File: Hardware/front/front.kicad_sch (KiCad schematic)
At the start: 53 parts, among them J101 Conn_02x10_Odd_Even, SW101 Alps EC11E, SW102 C&K-D6R-Illuminated, SW103 B3W-9002-Y1C, SW104 B3W-9002-Y1C, SW105 B3W-9002-Y1C, SW106 B3W-9002-Y1C, SW107 B3W-9000-RHG2C, U101 XRA1203, U102 AT24CS32-SSHM, U103 PCA9955B, U104 74LV14

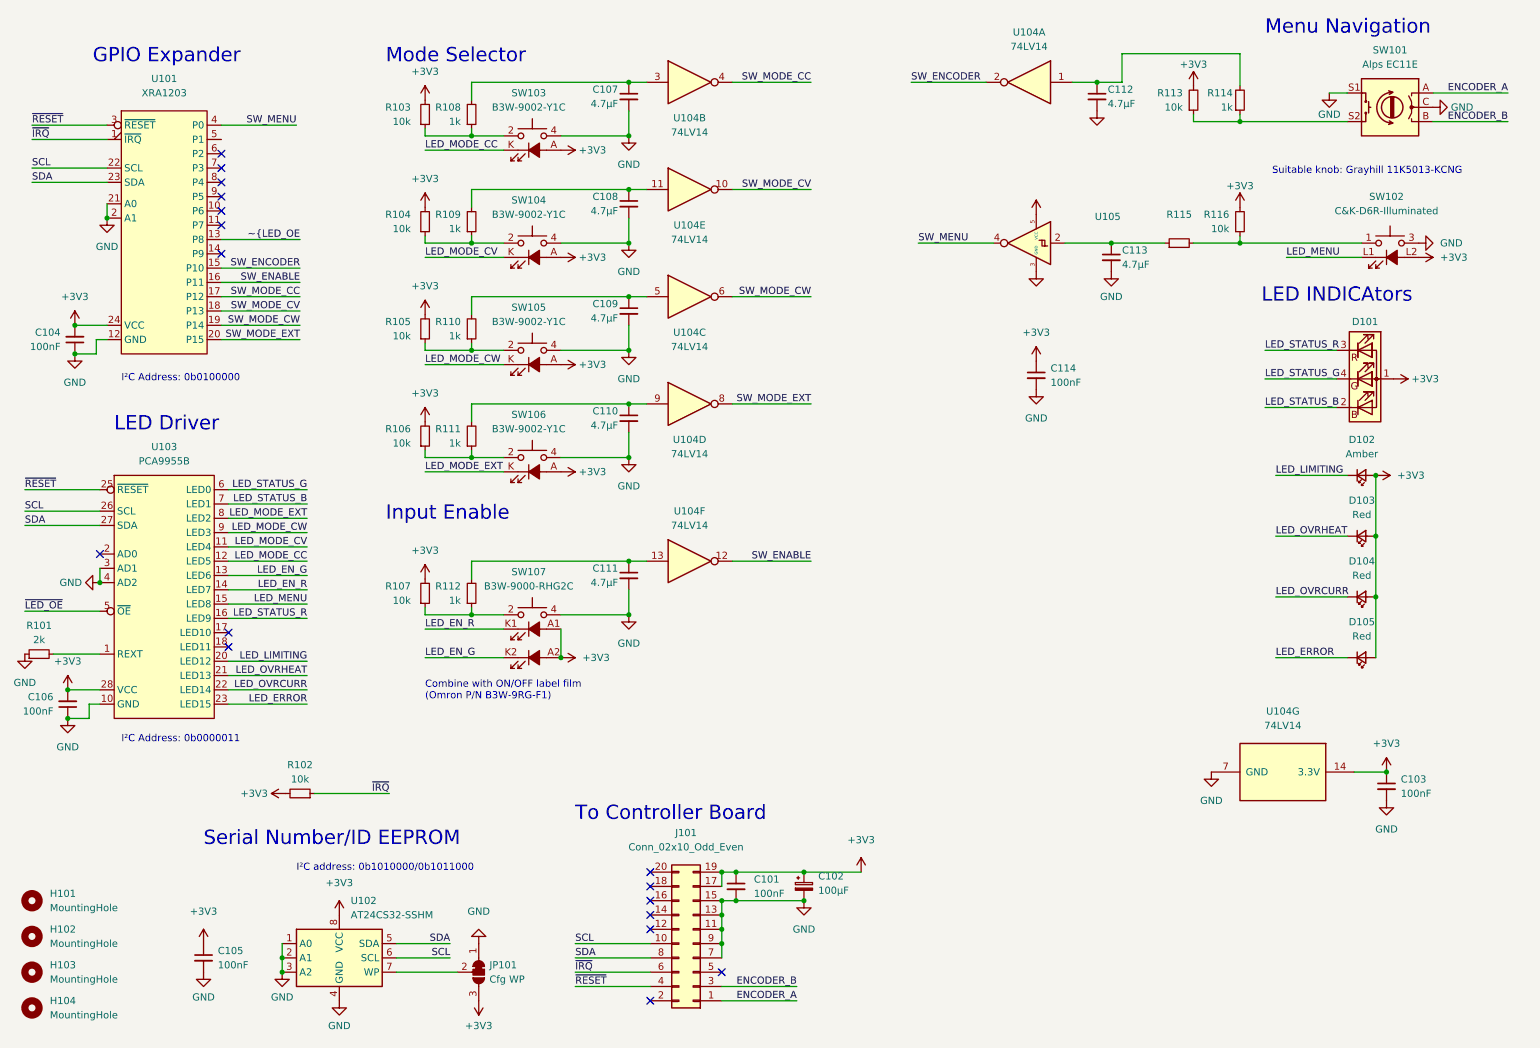
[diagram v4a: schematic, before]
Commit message: More tweaks to rev 2 front panel
- Added on-board pull ups for encoder lines, to reduce noise carried on
  the lines

- Cleaned up a few traces

- Actually fixed the footprint of the RGB LED so that not only does the
  common terminal match up, as do all three of the color terminals also
  :D
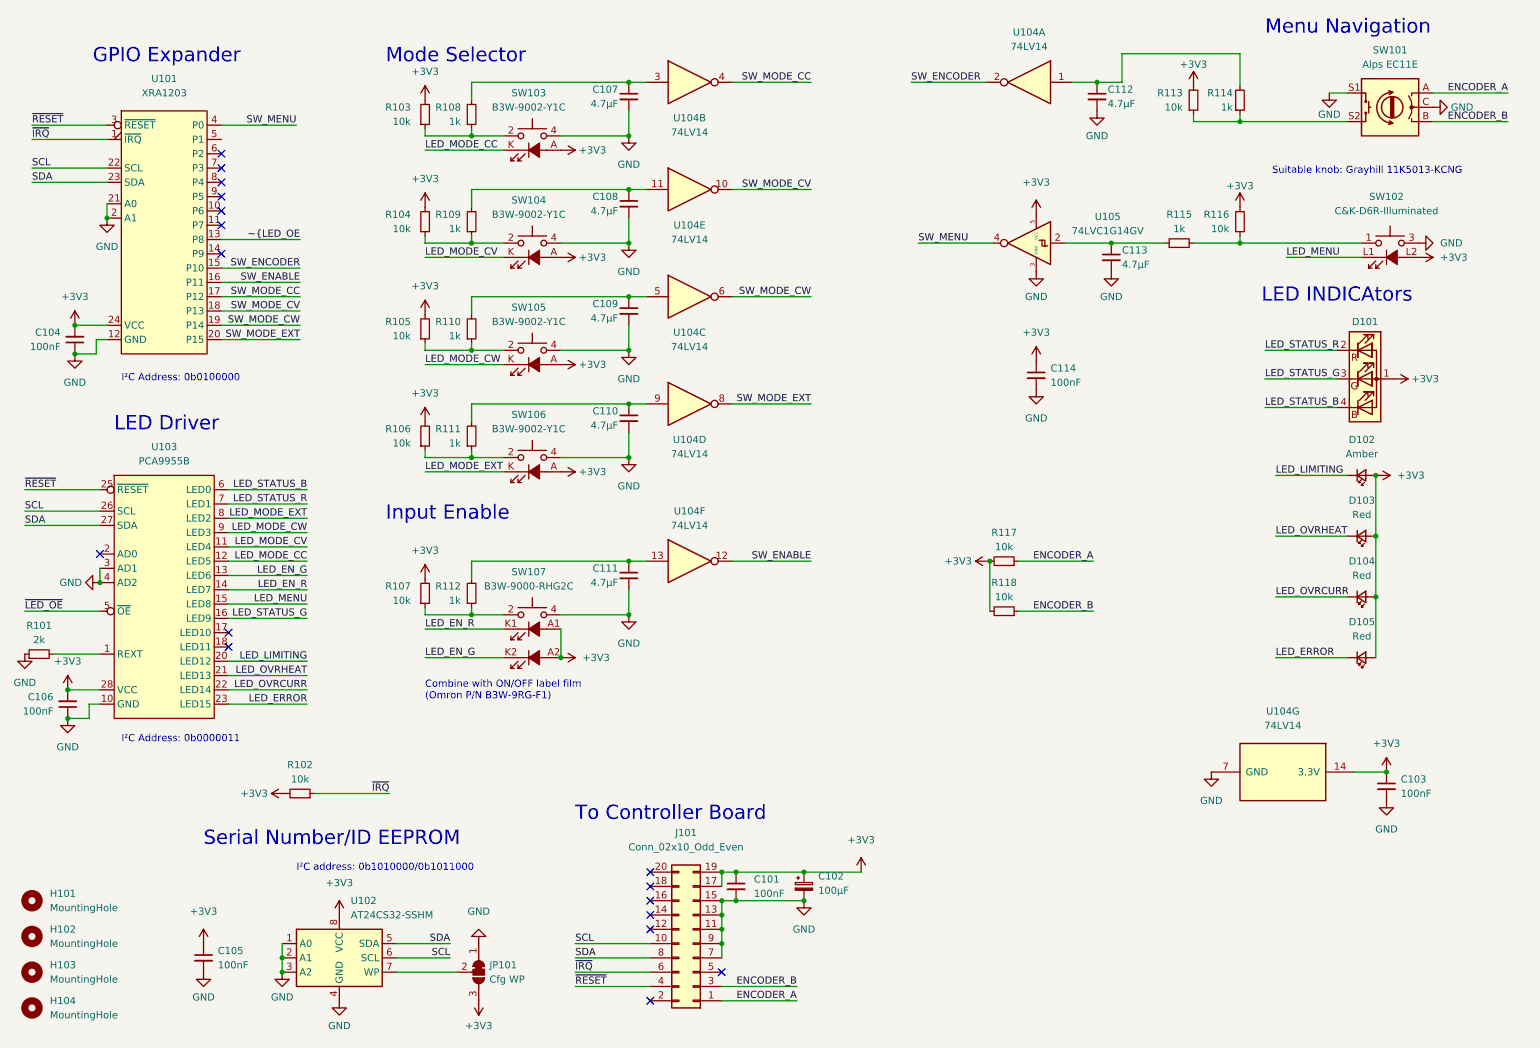
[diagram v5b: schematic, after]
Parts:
- added R117, R118: 10k, Resistor_SMD:R_0805_2012Metric_Pad1.20x1.40mm_HandSolder, symbol Device:R_Small
- D101: symbol Device:LED_ABRG -> Device:LED_ARGB
- R115: value (none) -> 1k; footprint (none) -> Resistor_SMD:R_0805_2012Metric_Pad1.20x1.40mm_HandSolder
- U105: value (none) -> 74LVC1G14GV; footprint (none) -> Package_TO_SOT_SMD:SOT-23-5
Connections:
- net +3V3: now also R117.2, R118.2
- net ENCODER_A: now also R117.1
- net ENCODER_B: now also R118.1
- net LED_STATUS_B: now also D101.4 (BK), U103.6 (LED0); no longer D101.2 (BK), U103.7 (LED1)
- net LED_STATUS_G: now also D101.3 (GK), U103.16 (LED9); no longer D101.4 (GK), U103.6 (LED0)
- net LED_STATUS_R: now also D101.2 (RK), U103.7 (LED1); no longer D101.3 (RK), U103.16 (LED9)
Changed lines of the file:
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@@
     (rev "1")
   )
+  (junction (at 189.23 111.125) (diameter 0) (color 0 0 0 0)
+  )
   (junction (at 97.155 35.56) (diameter 0) (color 0 0 0 0)
   )
@@
     (stroke (width 0) (type default) (color 0 0 0 0))
   )
+  (wire (pts (xy 207.645 111.125) (xy 194.31 111.125))
+    (stroke (width 0) (type default) (color 0 0 0 0))
+  )
   (wire (pts (xy 254 148.59) (xy 259.715 148.59))
     (stroke (width 0) (type default) (color 0 0 0 0))
@@
     (stroke (width 0) (type default) (color 0 0 0 0))
   )
+  (wire (pts (xy 189.23 111.125) (xy 189.23 120.015))
+    (stroke (width 0) (type default) (color 0 0 0 0))
+  )
   (wire (pts (xy 67.945 103.505) (xy 53.975 103.505))
     (stroke (width 0) (type default) (color 0 0 0 0))
@@
     (stroke (width 0) (type default) (color 0 0 0 0))
   )
+  (wire (pts (xy 207.645 120.015) (xy 194.31 120.015))
+    (stroke (width 0) (type default) (color 0 0 0 0))
+  )
   (wire (pts (xy 53.975 100.965) (xy 67.945 100.965))
     (stroke (width 0) (type default) (color 0 0 0 0))
@@
     (effects (font (size 1.27 1.27)) (justify left bottom))
   )
-  (label "LED_STATUS_B" (at 67.945 100.965 180)
+  (label "LED_STATUS_R" (at 67.945 100.965 180)
     (effects (font (size 1.27 1.27)) (justify right bottom))
   )
@@
     (effects (font (size 1.27 1.27)) (justify right bottom))
   )
+  (label "ENCODER_A" (at 207.645 111.125 180)
+    (effects (font (size 1.27 1.27)) (justify right bottom))
+  )
   (label "LED_LIMITING" (at 67.945 128.905 180)
     (effects (font (size 1.27 1.27)) (justify right bottom))
@@
     (effects (font (size 1.27 1.27)) (justify right bottom))
   )
-  (label "LED_STATUS_R" (at 67.945 121.285 180)
+  (label "LED_STATUS_G" (at 67.945 121.285 180)
     (effects (font (size 1.27 1.27)) (justify right bottom))
   )
@@
     (effects (font (size 1.27 1.27)) (justify left bottom))
   )
+  (label "ENCODER_B" (at 207.645 120.015 180)
+    (effects (font (size 1.27 1.27)) (justify right bottom))
+  )
   (label "SW_MODE_CW" (at 66.675 69.215 180)
     (effects (font (size 1.27 1.27)) (justify right bottom))
@@
     (effects (font (size 1.27 1.27)) (justify left bottom))
   )
-  (label "LED_STATUS_G" (at 67.945 98.425 180)
+  (label "LED_STATUS_B" (at 67.945 98.425 180)
     (effects (font (size 1.27 1.27)) (justify right bottom))
   )
@@
       (effects (font (size 1.27 1.27)) hide)
     )
-    (property "Value" "" (id 1) (at 197.485 43.815 0))
+    (property "Value" "+3V3" (id 1) (at 197.485 43.815 0))
     (property "Footprint" "" (id 2) (at 197.485 49.53 0)
       (effects (font (size 1.27 1.27)) hide)
@@
     (pin "2")
   )
-  (symbol (lib_id "Device:LED_ABRG") (at 255.905 78.74 0) (unit 1)
+  (symbol (lib_id "Device:LED_ARGB") (at 255.905 78.74 0) (unit 1)
     (in_bom yes) (on_board yes)
     (property "Reference" "D101" (id 0) (at 255.905 68.58 0))
@@
     (in_bom yes) (on_board yes) (fields_autoplaced)
     (property "Reference" "U105" (id 0) (at 210.185 49.911 0))
-    (property "Value" "" (id 1) (at 210.185 52.451 0))
-    (property "Footprint" "" (id 2) (at 197.485 60.96 0)
+    (property "Value" "74LVC1G14GV" (id 1) (at 210.185 52.451 0))
+    (property "Footprint" "Package_TO_SOT_SMD:SOT-23-5" (id 2) (at 197.485 60.96 0)
       (effects (font (size 1.27 1.27)) hide)
     )
@@
     (pin "1")
   )
+  (symbol (lib_id "power:+3V3") (at 189.23 111.125 90) (unit 1)
+    (in_bom yes) (on_board yes) (fields_autoplaced)
+    (property "Reference" "#PWR0150" (id 0) (at 193.04 111.125 0)
+      (effects (font (size 1.27 1.27)) hide)
+    )
+    (property "Value" "+3V3" (id 1) (at 186.055 111.1249 90)
+      (effects (font (size 1.27 1.27)) (justify left))
+    )
+    (property "Footprint" "" (id 2) (at 189.23 111.125 0)
+      (effects (font (size 1.27 1.27)) hide)
+    )
+    (property "Datasheet" "" (id 3) (at 189.23 111.125 0)
+      (effects (font (size 1.27 1.27)) hide)
+    )
+    (pin "1")
+  )
   (symbol (lib_id "programmable-load:XRA1203") (at 42.545 31.115 0) (unit 1)
     (in_bom yes) (on_board yes) (fields_autoplaced)
@@
     (in_bom yes) (on_board yes)
     (property "Reference" "R115" (id 0) (at 222.885 49.53 90))
-    (property "Value" "" (id 1) (at 222.885 52.07 90))
-    (property "Footprint" "" (id 2) (at 222.885 54.61 0)
+    (property "Value" "1k" (id 1) (at 222.885 52.07 90))
+    (property "Footprint" "Resistor_SMD:R_0805_2012Metric_Pad1.20x1.40mm_HandSolder" (id 2) (at 222.885 54.61 0)
       (effects (font (size 1.27 1.27)) hide)
     )
@@
     (pin "2")
   )
+  (symbol (lib_id "Device:R_Small") (at 191.77 120.015 270) (mirror x) (unit 1)
+    (in_bom yes) (on_board yes)
+    (property "Reference" "R118" (id 0) (at 191.77 114.935 90))
+    (property "Value" "10k" (id 1) (at 191.77 117.475 90))
+    (property "Footprint" "Resistor_SMD:R_0805_2012Metric_Pad1.20x1.40mm_HandSolder" (id 2) (at 191.77 120.015 0)
+      (effects (font (size 1.27 1.27)) hide)
+    )
+    (property "Datasheet" "~" (id 3) (at 191.77 120.015 0)
+      (effects (font (size 1.27 1.27)) hide)
+    )
+    (property "MPN" "RMC1/10-103JTP" (id 4) (at 191.77 120.015 90)
+      (effects (font (size 1.27 1.27)) hide)
+    )
+    (pin "1")
+    (pin "2")
+  )
   (symbol (lib_id "Device:C_Small") (at 210.82 57.15 0) (unit 1)
     (in_bom yes) (on_board yes)
@@
       (effects (font (size 1.27 1.27)) hide)
     )
-    (property "Value" "" (id 1) (at 197.485 64.135 0))
+    (property "Value" "GND" (id 1) (at 197.485 64.135 0))
     (property "Footprint" "" (id 2) (at 197.485 59.69 0)
       (effects (font (size 1.27 1.27)) hide)
@@
       (effects (font (size 1.27 1.27)) hide)
     )
-    (property "Value" "" (id 1) (at 208.28 35.56 0))
+    (property "Value" "GND" (id 1) (at 208.28 35.56 0))
     (property "Footprint" "" (id 2) (at 208.28 31.115 0)
       (effects (font (size 1.27 1.27)) hide)
@@
     (pin "2")
   )
+  (symbol (lib_id "Device:R_Small") (at 191.77 111.125 270) (mirror x) (unit 1)
+    (in_bom yes) (on_board yes)
+    (property "Reference" "R117" (id 0) (at 191.77 106.045 90))
+    (property "Value" "10k" (id 1) (at 191.77 108.585 90))
+    (property "Footprint" "Resistor_SMD:R_0805_2012Metric_Pad1.20x1.40mm_HandSolder" (id 2) (at 191.77 111.125 0)
+      (effects (font (size 1.27 1.27)) hide)
+    )
+    (property "Datasheet" "~" (id 3) (at 191.77 111.125 0)
+      (effects (font (size 1.27 1.27)) hide)
+    )
+    (property "MPN" "RMC1/10-103JTP" (id 4) (at 191.77 111.125 90)
+      (effects (font (size 1.27 1.27)) hide)
+    )
+    (pin "1")
+    (pin "2")
+  )
   (symbol (lib_id "power:GND") (at 31.115 114.935 270) (unit 1)
     (in_bom yes) (on_board yes) (fields_autoplaced)
@@
       (reference "#PWR0149") (unit 1) (value "GND") (footprint "")
     )
+    (path "/68dadee9-22bb-4cbe-aa25-79886e75d180"
+      (reference "#PWR0150") (unit 1) (value "+3V3") (footprint "")
+    )
     (path "/41415bac-1126-4467-b765-03fce423d075"
       (reference "C101") (unit 1) (value "100nF") (footprint "Capacitor_SMD:C_0805_2012Metric_Pad1.18x1.45mm_HandSolder")
@@
       (reference "R116") (unit 1) (value "10k") (footprint "Resistor_SMD:R_0805_2012Metric_Pad1.20x1.40mm_HandSolder")
     )
+    (path "/d7068e86-6312-4342-aa63-c1b7ad68015f"
+      (reference "R117") (unit 1) (value "10k") (footprint "Resistor_SMD:R_0805_2012Metric_Pad1.20x1.40mm_HandSolder")
+    )
+    (path "/89b6fd41-b642-443a-a9fa-f69b8f257087"
+      (reference "R118") (unit 1) (value "10k") (footprint "Resistor_SMD:R_0805_2012Metric_Pad1.20x1.40mm_HandSolder")
+    )
     (path "/99deab52-0fbc-4866-8276-198c86debfa9"

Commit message: Changed front panel rotary encoder
- Switched the Alps encoder for a part that's a quarter the price, and
  also uses gray code rather than quadrature encoding. This is a bit
  more ubiquitous and easier to parse
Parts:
- SW101: value Alps EC11E -> (none); footprint Rotary_Encoder:RotaryEncoder_Alps_EC11E-Switch_Vertical_H20mm -> (none); MPN EC11E18244AU -> EN11-HSM1AF15
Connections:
- net GND: now also SW101.S2; no longer SW101.S1
- net at R113.1, R114.1: now also SW101.S1; no longer SW101.S2
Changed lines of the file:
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@@
   (junction (at 156.21 166.37) (diameter 0) (color 0 0 0 0)
   )
-  (junction (at 233.68 33.02) (diameter 0) (color 0 0 0 0)
-  )
   (junction (at 97.155 54.61) (diameter 0) (color 0 0 0 0)
   )
+  (junction (at 233.68 33.02) (diameter 0) (color 0 0 0 0)
+  )
   (junction (at 156.21 171.45) (diameter 0) (color 0 0 0 0)
   )
@@
     (stroke (width 0) (type default) (color 0 0 0 0))
   )
+  (wire (pts (xy 238.76 33.02) (xy 238.76 27.94))
+    (stroke (width 0) (type default) (color 0 0 0 0))
+  )
   (wire (pts (xy 254 148.59) (xy 259.715 148.59))
     (stroke (width 0) (type default) (color 0 0 0 0))
@@
     (stroke (width 0) (type default) (color 0 0 0 0))
   )
-  (wire (pts (xy 249.555 27.94) (xy 252.73 27.94))
-    (stroke (width 0) (type default) (color 0 0 0 0))
-  )
   (wire (pts (xy 255.27 57.15) (xy 241.935 57.15))
     (stroke (width 0) (type default) (color 0 0 0 0))
@@
     (stroke (width 0) (type default) (color 0 0 0 0))
   )
-  (wire (pts (xy 233.68 33.02) (xy 252.73 33.02))
+  (wire (pts (xy 233.68 33.02) (xy 238.76 33.02))
     (stroke (width 0) (type default) (color 0 0 0 0))
   )
@@
     (stroke (width 0) (type default) (color 0 0 0 0))
   )
+  (wire (pts (xy 238.76 27.94) (xy 252.73 27.94))
+    (stroke (width 0) (type default) (color 0 0 0 0))
+  )
   (wire (pts (xy 157.48 83.185) (xy 143.51 83.185))
     (stroke (width 0) (type default) (color 0 0 0 0))
@@
     (in_bom yes) (on_board yes) (fields_autoplaced)
     (property "Reference" "SW101" (id 0) (at 260.35 20.32 0))
-    (property "Value" "Alps EC11E" (id 1) (at 260.35 22.86 0))
-    (property "Footprint" "Rotary_Encoder:RotaryEncoder_Alps_EC11E-Switch_Vertical_H20mm" (id 2) (at 264.16 26.416 0)
+    (property "Value" "" (id 1) (at 260.35 22.86 0))
+    (property "Footprint" "" (id 2) (at 264.16 26.416 0)
       (effects (font (size 1.27 1.27)) hide)
     )
@@
       (effects (font (size 1.27 1.27)) hide)
     )
-    (property "MPN" "EC11E18244AU" (id 4) (at 260.35 30.48 0)
+    (property "MPN" "EN11-HSM1AF15" (id 4) (at 260.35 30.48 0)
       (effects (font (size 1.27 1.27)) hide)
     )
@@
     (pin "L2")
   )
-  (symbol (lib_id "power:GND") (at 249.555 27.94 0) (mirror y) (unit 1)
+  (symbol (lib_id "power:GND") (at 252.73 33.02 0) (mirror y) (unit 1)
     (in_bom yes) (on_board yes)
-    (property "Reference" "#PWR0125" (id 0) (at 249.555 34.29 0)
+    (property "Reference" "#PWR0125" (id 0) (at 252.73 39.37 0)
       (effects (font (size 1.27 1.27)) hide)
     )
-    (property "Value" "GND" (id 1) (at 249.555 31.75 0))
-    (property "Footprint" "" (id 2) (at 249.555 27.94 0)
+    (property "Value" "GND" (id 1) (at 252.73 36.83 0))
+    (property "Footprint" "" (id 2) (at 252.73 33.02 0)
       (effects (font (size 1.27 1.27)) hide)
     )
-    (property "Datasheet" "" (id 3) (at 249.555 27.94 0)
+    (property "Datasheet" "" (id 3) (at 252.73 33.02 0)
       (effects (font (size 1.27 1.27)) hide)
     )
@@
     )
     (path "/99deab52-0fbc-4866-8276-198c86debfa9"
-      (reference "SW101") (unit 1) (value "Alps EC11E") (footprint "Rotary_Encoder:RotaryEncoder_Alps_EC11E-Switch_Vertical_H20mm")
+      (reference "SW101") (unit 1) (value "TT EN11") (footprint "programmable-load:TT_Electronics-EN11-HSM1AF15-0")
     )
     (path "/c748ca36-6c04-4ba0-a4b6-196d9bddcb36"

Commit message: Added front/rear panel files
- Added CAD files for the front and rear panels for the programmable
  load. These are meant to go with a Hammond 1598JBK enclosure.
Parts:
- SW101: MPN EN11-HSM1AF15 -> EN11-HSM1AF25
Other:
- note added: "Suitable knob: Grayhill 11K5013-KCNG or Eagle Plastic Devices 450-2925"
- note removed: "Suitable knob: Grayhill 11K5013-KCNG"
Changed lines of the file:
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@@
     (title "Front Panel")
     (date "2022-03-07")
-    (rev "1")
+    (rev "2")
   )
   (junction (at 189.23 111.125) (diameter 0) (color 0 0 0 0)
@@
     (effects (font (size 2.54 2.54)) (justify left bottom))
   )
-  (text "Suitable knob: Grayhill 11K5013-KCNG" (at 239.395 42.545 0)
+  (text "Suitable knob: Grayhill 11K5013-KCNG\nor Eagle Plastic Devices 450-2925"
+    (at 239.395 43.18 0)
     (effects (font (size 1.27 1.27)) (justify left bottom))
   )
@@
       (effects (font (size 1.27 1.27)) hide)
     )
-    (property "MPN" "EN11-HSM1AF15" (id 4) (at 260.35 30.48 0)
-      (effects (font (size 1.27 1.27)) hide)
-    )
+    (property "MPN" "EN11-HSM1AF25" (id 4) (at 260.35 30.48 0)
+      (effects (font (size 1.27 1.27)) hide)
+    )

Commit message: Rear IO rework
- Mostly finished the rear IO board rework (adding the CAN filtering and
  switchable termination; trigger input pulse shaper; fuses for
  expansion +12V)

- Changed encoder type on front panel for a shorter type

- Created schematic models and footprints for Bournds DR311 chokes;
  Mill-Max 2108 solder turrets
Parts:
- SW101: MPN EN11-HSM1AF25 -> EN11-HSM1BF20
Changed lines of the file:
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@@
       (effects (font (size 1.27 1.27)) hide)
     )
-    (property "MPN" "EN11-HSM1AF25" (id 4) (at 260.35 30.48 0)
+    (property "MPN" "EN11-HSM1BF20" (id 4) (at 260.35 30.48 0)
       (effects (font (size 1.27 1.27)) hide)
     )
